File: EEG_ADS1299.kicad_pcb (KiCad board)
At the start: 2 copper layers, 48.5 x 21.7 mm, 68 parts, among them IC1 ADS1299, P1 CONN_2, P2 CONN_2, P3 CONN_01X06, U1 TPS61221, U2 TPS61222, U3 NRF528XX-QFAA, U4 MPU-9250, U5 INA828, U6 INA828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

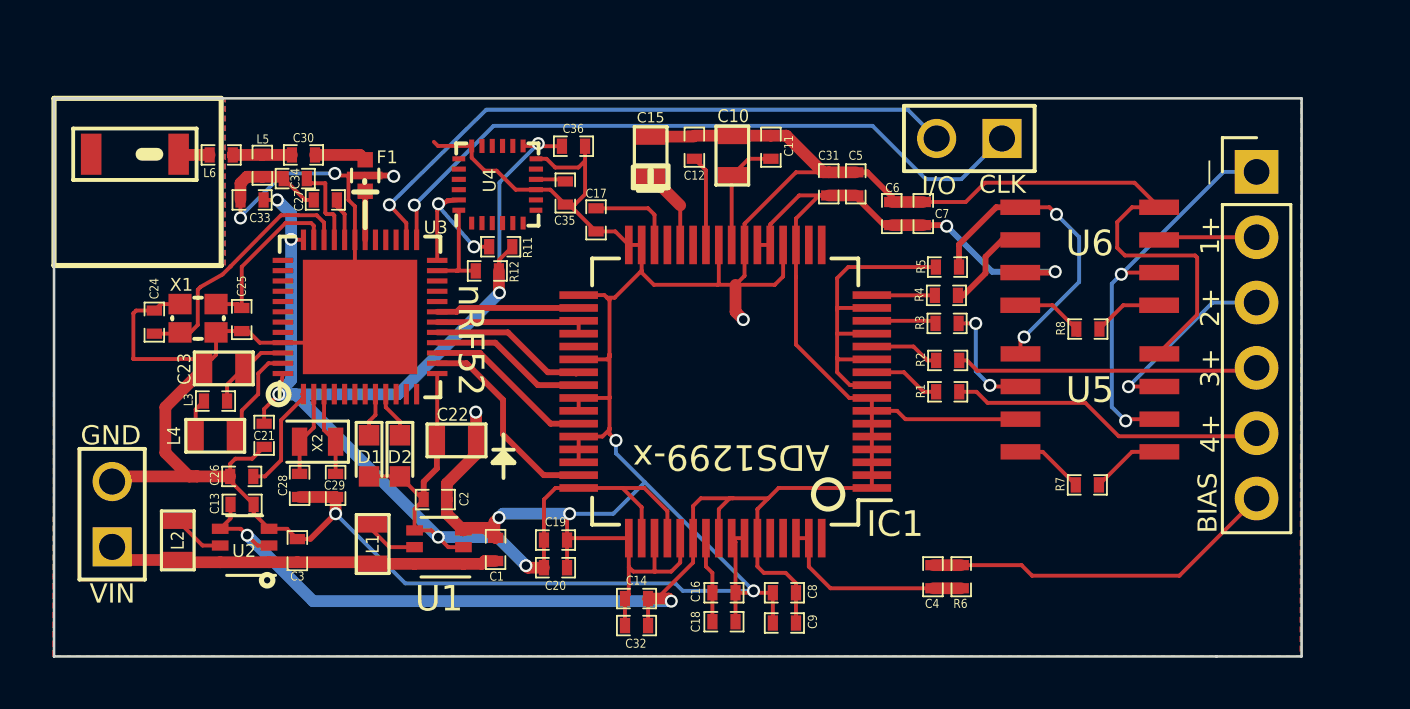
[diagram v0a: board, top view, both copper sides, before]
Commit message: (#1) - Added single capacitor on amp inputs. (C37)
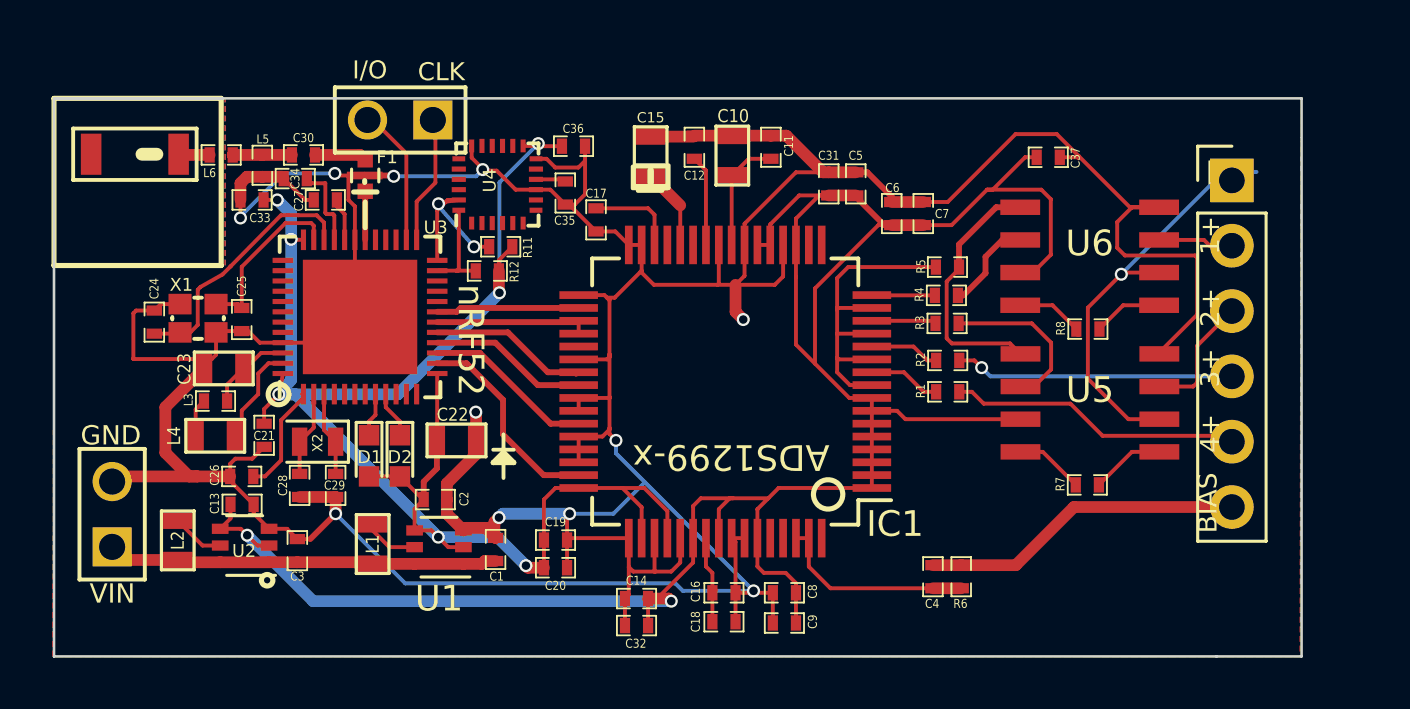
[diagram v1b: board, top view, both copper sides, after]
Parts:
- added C37: 1uF, SM0402, F.Cu at (304.6, 127.8)
- moved P2 22.1 mm to (279.4, 126.3)
- moved P3 1.02 mm to (311.7, 128.7)
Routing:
- net /SWDCLK: track 27.3 -> 5.27 mm, vias 1 -> 0
- net /SWDIO: track 24.9 -> 5.41 mm, vias 1 -> 0
- net AVDD: track 78.2 -> 89.6 mm, vias 4 -> 2
- net AVSS: track 203.5 -> 208.6 mm, vias 10 -> 11
- net /IN2: track 7.54 -> 4.87 mm, vias 1 -> 0
- net /INN-: track 12.1 -> 9.95 mm, vias 2 -> 0
- net Net-(R3-Pad2): track 4.51 -> 6.41 mm, vias 2 -> 0
- net /BIASIN: track 14.0 -> 12.6 mm
- net /IN3: track 12.2 -> 10.9 mm, vias 0 -> 1
- net /IN4: track 12.3 -> 11.4 mm
- net /IN1: track 3.83 -> 3.07 mm
- net /NEG_INPUT: track 15.8 -> 16.4 mm, vias 2 -> 1

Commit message: Added TPS63001, TPS22941.
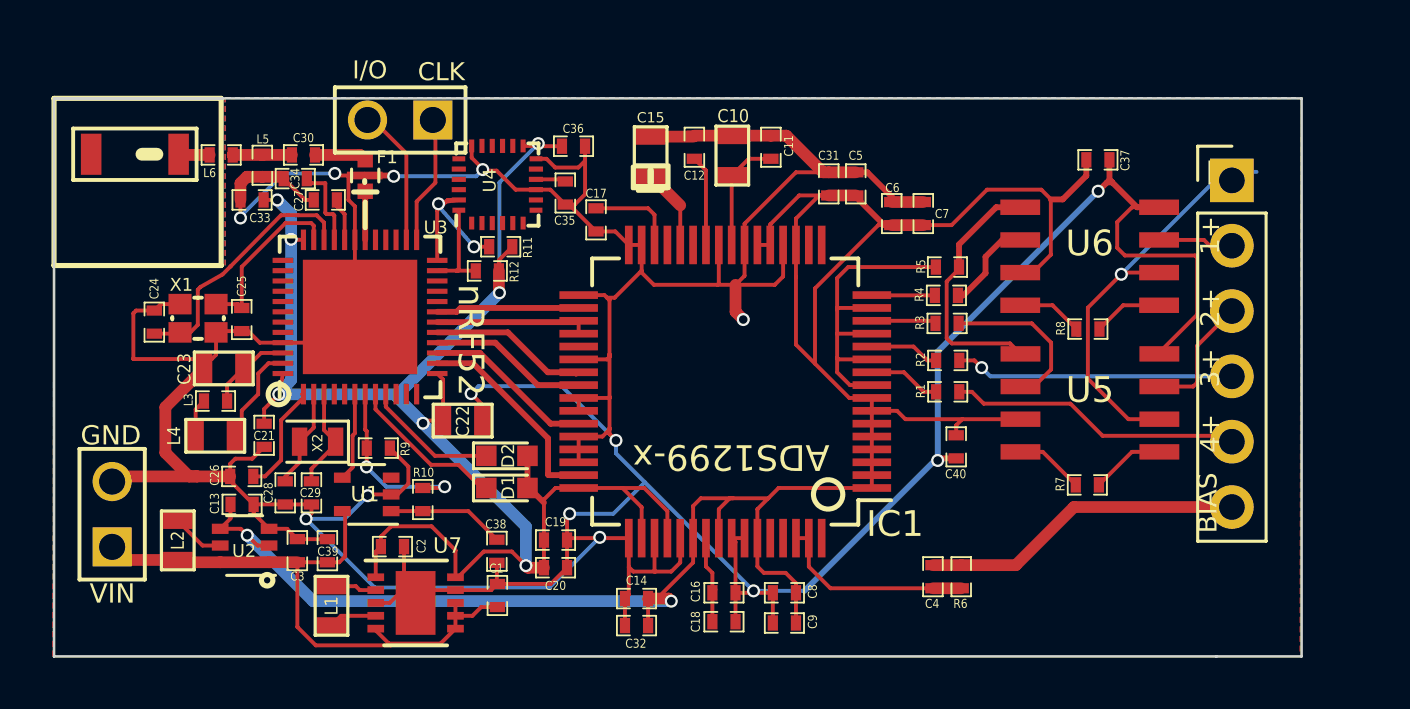
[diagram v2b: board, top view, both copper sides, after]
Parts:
- added C38: 10uF, SM0402, F.Cu at (283.1, 143.1)
- added C39: 10uF, SM0402, F.Cu at (276.5, 143.1)
- added C40: 1uF, SM0402, F.Cu at (301.0, 139.1)
- added R10: 1M, SM0402, F.Cu at (280.2, 141.1)
- added R9: 1M, SM0402, F.Cu at (278.5, 139.1)
- added U7: TPS63001, Housings_DFN_QFN:DFN-10-1EP_3x3mm_Pitch0.5mm, F.Cu at (280.0, 145.1)
- L1: value 4.7µH -> 2.2µH
- U1: value TPS61221 -> TPS2294x; footprint TO_SOT_Packages_SMD:SOT-363_SC-70-6 -> TO_SOT_Packages_SMD:SOT-353_SC-70-5
- moved D1 5.50 mm to (283.5, 140.7), turned to 0 degrees
- moved D2 4.16 mm to (283.5, 139.4), turned to 0 degrees
- moved U1 3.48 mm to (278.1, 140.9)
- moved L1 2.88 mm to (276.7, 145.2), turned to 90 degrees
- moved C2 2.47 mm to (279.1, 142.9)
- moved C37 1.93 mm to (306.5, 127.9)
- moved C1 1.79 mm to (283.1, 144.8), turned to 270 degrees
- moved C29 0.98 mm to (275.9, 140.8)
- moved C22 0.81 mm to (281.8, 138.0)
- moved C28 0.63 mm to (274.9, 140.8)
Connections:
- C1 pad 1: VCC -> AVSS
- C1 pad 2: AVSS -> VCC
- L1 pad 2: VCC -> Net-(L1-Pad2)
- U1 pad 1: VCC -> /Vout
- U1 pad 2: DVDD -> AVSS
- U1 pad 3: AVSS -> Net-(U1-Pad3)
- U1 pad 4: DVDD -> /LOAD_SW_CTRL
- U1 pad 5: Net-(L1-Pad1) -> VCC
- U3 pad 6: Net-(U3-Pad6) -> /LOAD_SW_CTRL
- U3 pad 7: Net-(U3-Pad7) -> /AIN_BAT_DIV_VOLTAGE
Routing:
- net AVSS: track 208.6 -> 235.5 mm, vias 11 -> 14
- net VCC: track 15.7 -> 24.8 mm
- net /AIN_BAT_DIV_VOLTAGE: track 0.00 -> 7.09 mm, vias 0 -> 2
- net /Vout: track 0.00 -> 4.57 mm
- net /LED2: track 1.70 -> 6.17 mm
- net /LOAD_SW_CTRL: track 0.00 -> 3.45 mm
- net /LED3: track 1.83 -> 5.19 mm
- net Net-(L1-Pad2): track 0.00 -> 1.78 mm
- net Net-(C29-Pad1): track 3.29 -> 3.97 mm
- net AVDD: track 89.6 -> 90.3 mm
- net Net-(C28-Pad1): track 3.33 -> 3.85 mm

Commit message: Fixed design and separated channels 1 and 2 from 3 and 4, with 1 and 2 being the pre-amplified circuits.
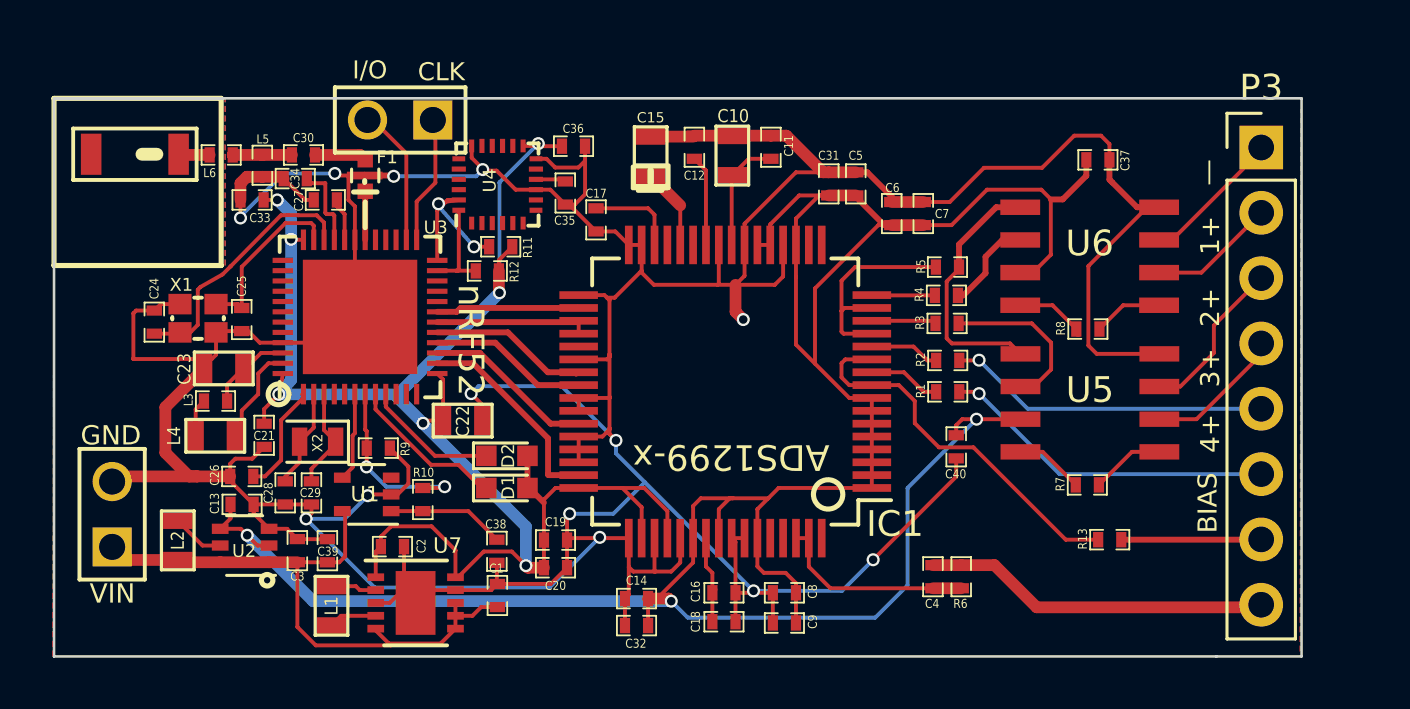
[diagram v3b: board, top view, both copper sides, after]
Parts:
- added R13: 30k, SM0402, F.Cu at (306.9, 142.7)
- P3: value CONN_01X06 -> CONN_01X08; footprint Pin_Headers:Pin_Header_Straight_1x06_Pitch2.54mm -> Pin_Headers:Pin_Header_Straight_1x08_Pitch2.54mm
- moved P3 1.71 mm to (312.8, 127.4)
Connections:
- net /INN- renamed /IN12-
- IC1 pad 11: /IN1- -> /IN3N
- IC1 pad 13: /IN1- -> /IN1N
- IC1 pad 15: /IN1- -> /IN1N
- IC1 pad 9: /IN1- -> /IN3N
- P3 pad 1: /NEG_INPUT -> /IN1
- P3 pad 2: /IN1 -> /IN1-
- P3 pad 4: /IN3 -> /IN2-
- P3 pad 5: /IN4 -> /IN3
- P3 pad 6: /BIASIN -> /IN4
- R5 pad 1: /IN1- -> /IN1N
- U5 pad 2: /NEG_INPUT -> /IN2-
- U6 pad 2: /NEG_INPUT -> /IN1-
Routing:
- net /NEG_INPUT: track 16.4 -> 0.00 mm, vias 1 -> 0
- net /IN3N: track 0.00 -> 15.0 mm
- net AVDD: track 90.3 -> 104.2 mm, vias 2 -> 3
- net /IN1-: track 13.5 -> 4.93 mm
- net /IN1N: track 0.00 -> 8.31 mm
- net /IN34-: track 0.00 -> 5.44 mm
- net /IN2-: track 0.00 -> 5.43 mm
- net AVSS: track 235.5 -> 230.4 mm, vias 14 -> 13
- net /IN1: track 3.07 -> 5.68 mm
- net /IN3: track 10.9 -> 12.5 mm
- net /IN4: track 11.4 -> 13.1 mm, vias 0 -> 1
- net /IN2: track 4.87 -> 6.33 mm
- net /BIASIN: track 12.6 -> 13.5 mm

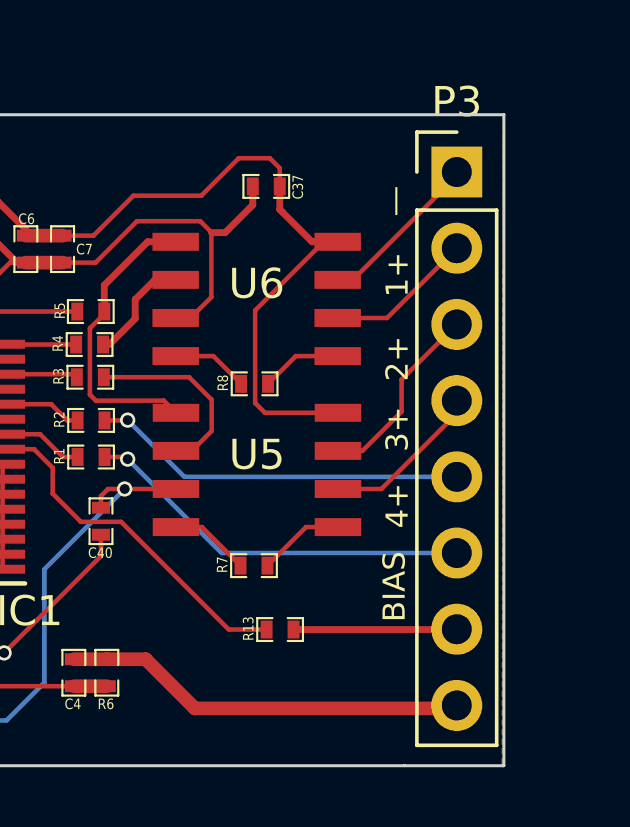
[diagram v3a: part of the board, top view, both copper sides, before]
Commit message: Updated front mask for correct information + gerber files for v3.2
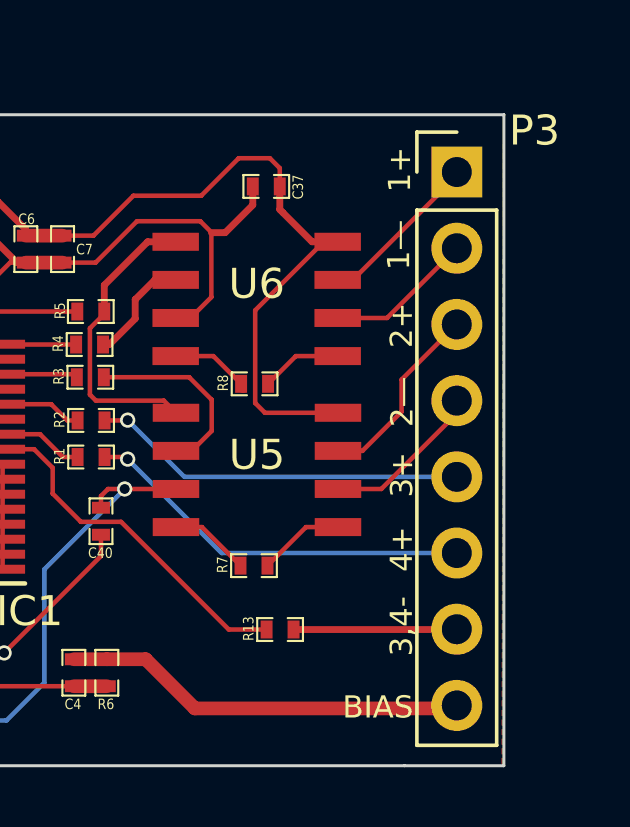
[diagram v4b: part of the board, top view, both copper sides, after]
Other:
- board text added: "1—"
- board text added: "2—"
- board text added: "3,4-"
- board text removed: "—"
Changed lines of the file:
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@@
-(kicad_pcb (version 4) (host pcbnew 4.0.4-stable)
+(kicad_pcb (version 4) (host pcbnew 4.0.6)
   (general
     (links 229)
     (no_connects 0)
-    (area 265.849999 125.449999 314.460001 147.250001)
+    (area 265.799999 122.157123 320.907143 148.7224)
     (thickness 1.6)
-    (drawings 30)
+    (drawings 32)
     (tracks 725)
     (zones 0)
@@
   )
   (setup
-    (last_trace_width 0.229)
+    (last_trace_width 0.4572)
     (user_trace_width 0.152)
     (user_trace_width 0.229)
@@
       (drillshape 0)
       (scaleselection 1)
-      (outputdirectory Gerber_nRF52_ExG_v3.1/))
+      (outputdirectory Gerber_nRF52_ExG_v3.2/))
   )
   (net 0 "")
@@
     (descr "Through hole straight pin header, 1x08, 2.54mm pitch, single row")
     (tags "Through hole pin header THT 1x08 2.54mm single row")
-    (fp_text reference P3 (at 0 -2.33) (layer F.SilkS)
+    (fp_text reference P3 (at 2.59 -1.38) (layer F.SilkS)
       (effects (font (size 1 1) (thickness 0.15)))
     )
@@
     )
   )
-  (gr_text 4+ (at 310.86 138.53 90) (layer F.SilkS)
+  (gr_text BIAS (at 310.21 145.25) (layer F.SilkS)
     (effects (font (size 0.74 0.75) (thickness 0.1)))
   )
-  (gr_text 3+ (at 310.86 135.98 90) (layer F.SilkS)
+  (gr_text 3,4- (at 311 142.55 90) (layer F.SilkS)
     (effects (font (size 0.74 0.75) (thickness 0.1)))
   )
-  (gr_text 2+ (at 310.86 133.63 90) (layer F.SilkS)
+  (gr_text 4+ (at 311 139.98 90) (layer F.SilkS)
+    (effects (font (size 0.74 0.75) (thickness 0.1)))
+  )
+  (gr_text 3+ (at 311.01 137.5 90) (layer F.SilkS)
+    (effects (font (size 0.74 0.75) (thickness 0.1)))
+  )
+  (gr_text 2— (at 311.02 135.07 90) (layer F.SilkS)
+    (effects (font (size 0.74 0.75) (thickness 0.1)))
+  )
+  (gr_text 2+ (at 311 132.52 90) (layer F.SilkS)
+    (effects (font (size 0.74 0.75) (thickness 0.1)))
+  )
+  (gr_text 1+ (at 310.94 127.33 90) (layer F.SilkS)
     (effects (font (size 0.74 0.75) (thickness 0.1)))
   )
@@
     (effects (font (size 0.75 0.75) (thickness 0.1)))
   )
-  (gr_text 1+ (at 310.86 130.83 90) (layer F.SilkS)
-    (effects (font (size 0.74 0.75) (thickness 0.1)))
-  )
   (gr_line (start 277.55 129.14) (end 278.46 129.14) (angle 90) (layer F.SilkS) (width 0.2))
   (gr_line (start 277.98 128.77) (end 277.98 128.7) (angle 90) (layer F.SilkS) (width 0.2))
   (gr_line (start 278 130.53) (end 278 129.53) (angle 90) (layer F.SilkS) (width 0.2))
-  (gr_text — (at 310.76 128.38 90) (layer F.SilkS)
+  (gr_text 1— (at 310.91 129.84 90) (layer F.SilkS)
     (effects (font (size 0.74 0.75) (thickness 0.1)))
   )
@@
     (effects (font (size 1 1) (thickness 0.125)))
   )
-  (gr_text BIAS (at 310.76 141.23 90) (layer F.SilkS)
-    (effects (font (size 0.74 0.75) (thickness 0.1)))
-  )
   (gr_circle (center 274.1875 144.2375) (end 273.9875 144.1375) (layer F.SilkS) (width 0.2))
   (gr_circle (center 296 140.9) (end 296.45 141.25) (layer F.SilkS) (width 0.2))
@@
     (connect_pads (clearance 0.508))
     (min_thickness 0.254)
-    (fill yes (arc_segments 16) (thermal_gap 0.508) (thermal_bridge_width 0.508))
+    (fill (arc_segments 16) (thermal_gap 0.508) (thermal_bridge_width 0.508))
     (polygon
       (pts
@@
     (connect_pads (clearance 0.508))
     (min_thickness 0.254)
-    (fill yes (arc_segments 16) (thermal_gap 0.508) (thermal_bridge_width 0.508))
+    (fill (arc_segments 16) (thermal_gap 0.508) (thermal_bridge_width 0.508))
     (polygon
       (pts
